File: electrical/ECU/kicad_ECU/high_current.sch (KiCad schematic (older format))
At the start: 5 parts

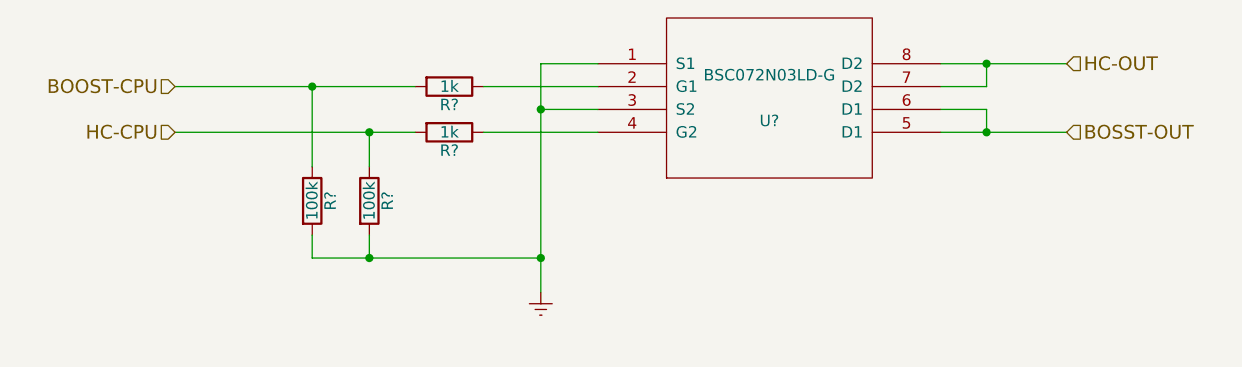
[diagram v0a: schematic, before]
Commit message: fixed some naming errors and initial round of double checking
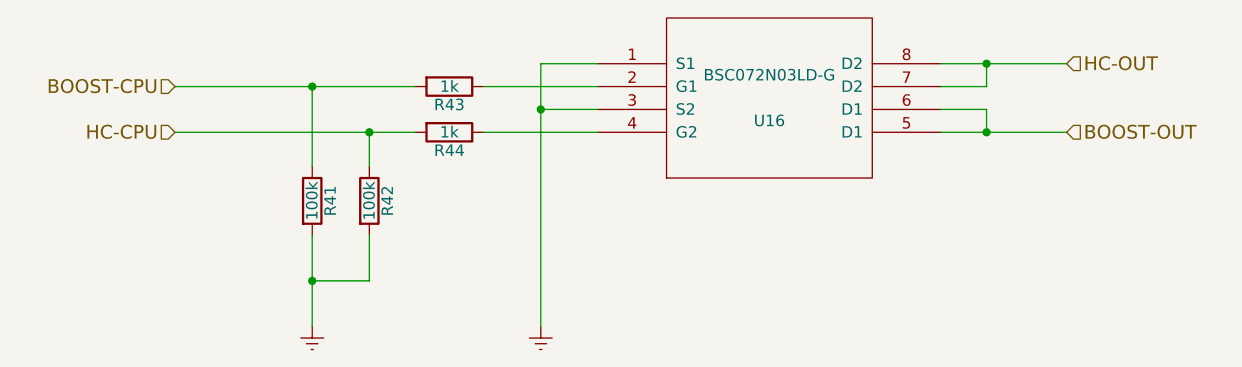
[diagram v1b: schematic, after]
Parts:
- gave numbers to parts that had none: 5
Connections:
- net BOSST-OUT renamed BOOST-OUT
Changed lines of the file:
@@
 $Descr A4 11693 8268
 encoding utf-8
-Sheet 17 33
+Sheet 21 33
 Title "High current drains"
 Date ""
@@
 $EndDescr
 $Comp
-L BSC072N03LD-G U?
+L BSC072N03LD-G U16
 U 1 1 5977C2D7
 P 6600 3150
-F 0 "U?" H 6600 3050 50  0000 C CNN
+F 0 "U16" H 6600 3050 50  0000 C CNN
 F 1 "BSC072N03LD-G" H 6600 3250 50  0000 C CNN
 F 2 "MODULE" H 6600 3150 50  0001 C CNN
@@
 $EndComp
 $Comp
-L Earth #PWR?
-U 1 1 5977C2DE
-P 5600 4000
-F 0 "#PWR?" H 5600 3750 50  0001 C CNN
-F 1 "Earth" H 5600 3850 50  0001 C CNN
-F 2 "" H 5600 4000 50  0001 C CNN
-F 3 "" H 5600 4000 50  0001 C CNN
-	1    5600 4000
-	1    0    0    -1
-$EndComp
-$Comp
-L R R?
+L R R43
 U 1 1 5977C2E4
 P 5200 3100
-F 0 "R?" V 5280 3100 50  0000 C CNN
+F 0 "R43" V 5280 3100 50  0000 C CNN
 F 1 "1k" V 5200 3100 50  0000 C CNN
 F 2 "" V 5130 3100 50  0001 C CNN
@@
 $EndComp
 $Comp
-L R R?
+L R R44
 U 1 1 5977C2EB
 P 5200 3300
-F 0 "R?" V 5280 3300 50  0000 C CNN
+F 0 "R44" V 5280 3300 50  0000 C CNN
 F 1 "1k" V 5200 3300 50  0000 C CNN
 F 2 "" V 5130 3300 50  0001 C CNN
@@
 $EndComp
 $Comp
-L R R?
+L R R42
 U 1 1 5977C2F2
 P 4850 3600
-F 0 "R?" V 4930 3600 50  0000 C CNN
+F 0 "R42" V 4930 3600 50  0000 C CNN
 F 1 "100k" V 4850 3600 50  0000 C CNN
 F 2 "" V 4780 3600 50  0001 C CNN
@@
 $EndComp
 $Comp
-L R R?
+L R R41
 U 1 1 5977C2F9
 P 4600 3600
-F 0 "R?" V 4680 3600 50  0000 C CNN
+F 0 "R41" V 4680 3600 50  0000 C CNN
 F 1 "100k" V 4600 3600 50  0000 C CNN
 F 2 "" V 4530 3600 50  0001 C CNN
@@
 Wire Wire Line
 	5850 3000 5600 3000
-Wire Wire Line
-	5600 3000 5600 4000
 Wire Wire Line
 	5850 3200 5600 3200
@@
 Connection ~ 4600 3100
 Wire Wire Line
-	4600 3750 4600 3850
+	4600 3750 4600 4150
 Wire Wire Line
-	4600 3850 5600 3850
-Connection ~ 5600 3850
-Wire Wire Line
-	4850 3750 4850 3850
-Connection ~ 4850 3850
+	4850 3750 4850 3950
 Wire Wire Line
 	7550 3100 7350 3100
@@
 HC-OUT
 Text HLabel 7900 3300 2    60   Input ~ 0
-BOSST-OUT
+BOOST-OUT
 Wire Wire Line
 	7550 3000 7550 3100
 Wire Wire Line
 	7550 3200 7550 3300
+$Comp
+L Earth #PWR49
+U 1 1 599401D9
+P 4600 4150
+F 0 "#PWR49" H 4600 3900 50  0001 C CNN
+F 1 "Earth" H 4600 4000 50  0001 C CNN
+F 2 "" H 4600 4150 50  0001 C CNN
+F 3 "" H 4600 4150 50  0001 C CNN
+	1    4600 4150
+	1    0    0    -1
+$EndComp
+$Comp
+L Earth #PWR50
+U 1 1 599401F7
+P 5600 4150
+F 0 "#PWR50" H 5600 3900 50  0001 C CNN
+F 1 "Earth" H 5600 4000 50  0001 C CNN
+F 2 "" H 5600 4150 50  0001 C CNN
+F 3 "" H 5600 4150 50  0001 C CNN
+	1    5600 4150
+	1    0    0    -1
+$EndComp
+Wire Wire Line
+	5600 3000 5600 4150
+Wire Wire Line
+	4850 3950 4600 3950
+Connection ~ 4600 3950
 $EndSCHEMATC
